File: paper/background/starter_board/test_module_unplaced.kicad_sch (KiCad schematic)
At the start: 15 parts, among them J1 Barrel_Jack_12V, M1 ERM_Motor, M2 Stepper_4wire, M3 Servo_3pin, U1 D24V22F5_Buck, U2 Pi_Pico_W, U3 DRV2605L_Breakout, U4 DRV8871_Breakout, U5 Tic_T500, U6 Waveshare_2CH_RS232

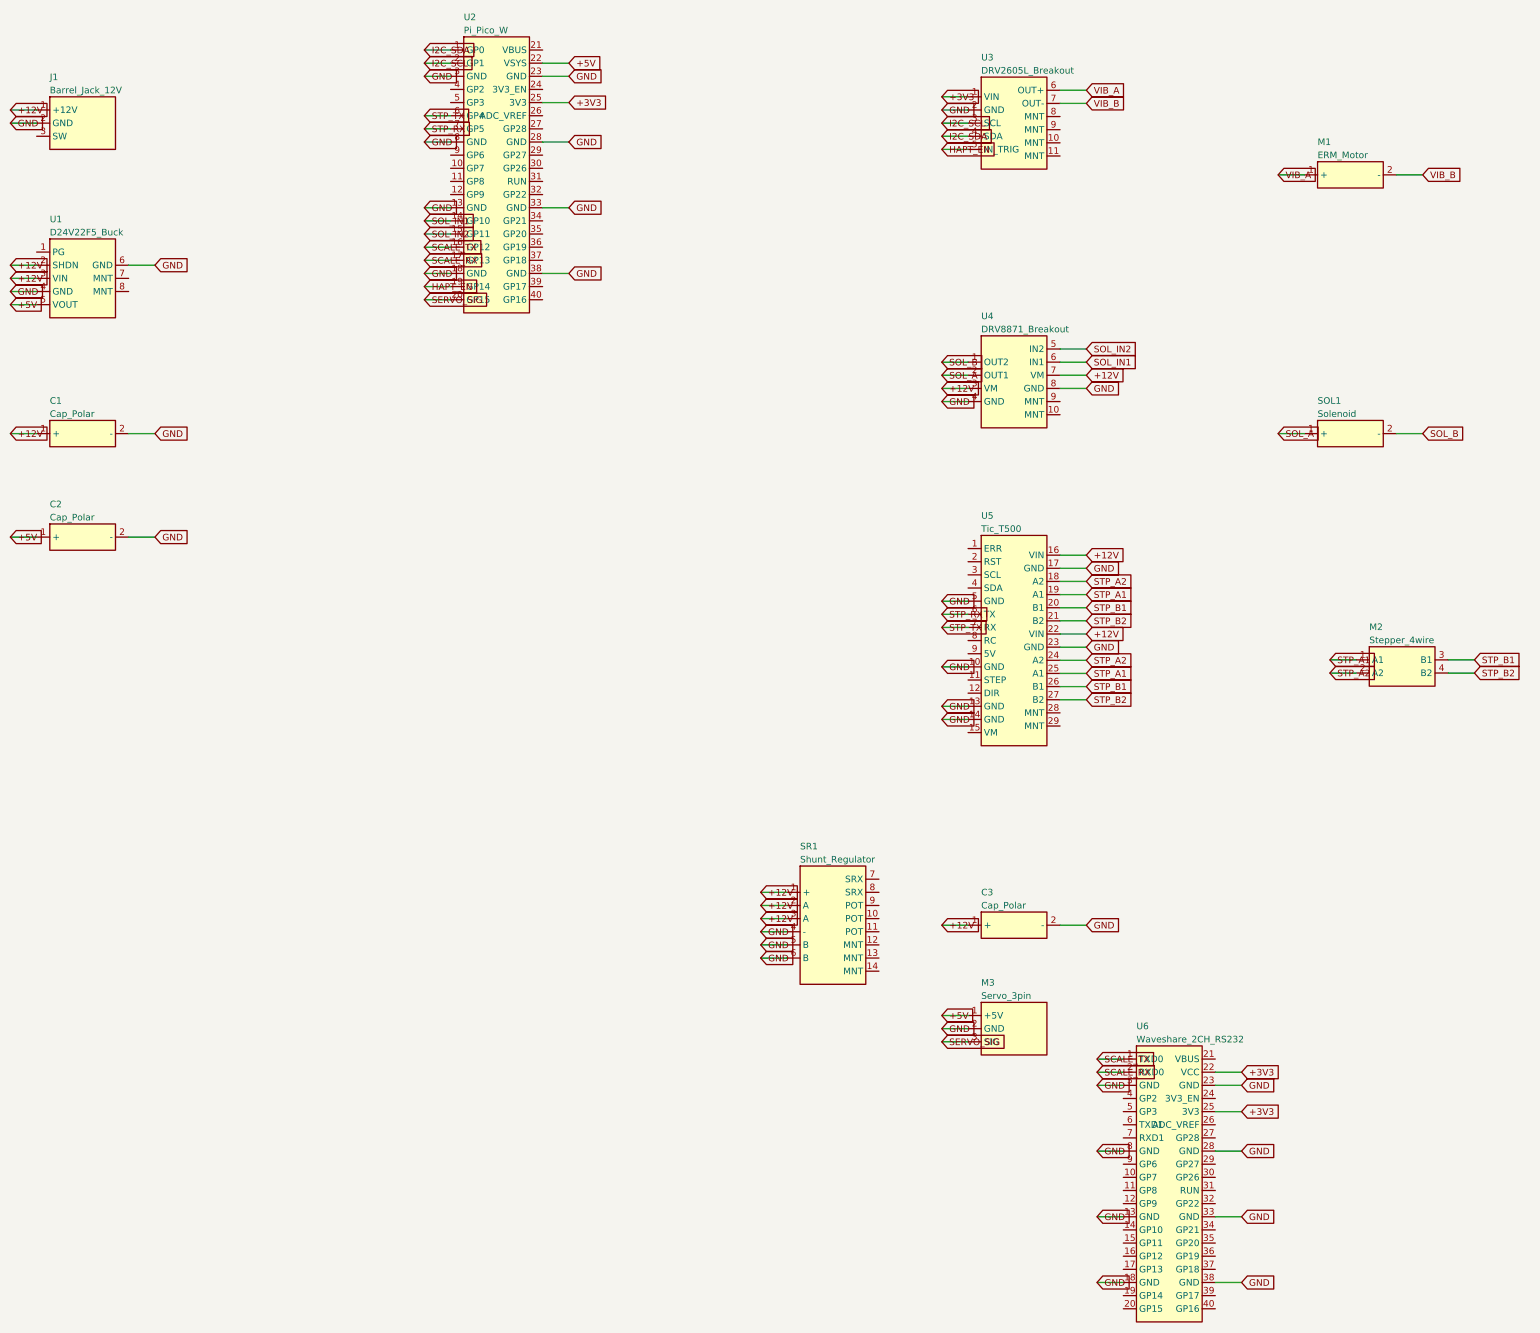
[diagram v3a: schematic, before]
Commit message: Add second dispensing-angle servo M4 (SERVO_SIG2 on GP2) — 2-servo design alignment
williamulbz's PR #76 review flagged that the board predates the move to
the 2-servo design (PR #66 dual-servo hinge; PR #100 generate.py rev C).
build_starter_board.py now emits a second 3-pin servo header M4 wired
exactly as rev C: SIG -> SERVO_SIG2 on Pico GP2 (mirrored in firmware via
config.SERVO2_INVERT), +5V/GND shared. M4 joins the logic/mcu placement
cluster beside M3, edge-biased for cable exit.

Counts: 16 footprints / 175 pads / 99 net-assigned / 23 nets (placed
outline ~162x85 mm; unplaced stays 110x110 mm at ~51% courtyard).
Verified: kicad-cli netlist 99 pins / 23 nets / zero unconnected on both
trios (SERVO_SIG2 = M4.3 <-> U2.4/GP2), pcbnew DRC clean (no courtyard/
clearance/short errors), 16<->16 footprint<->symbol UUID bijection,
byte-for-byte reproducible, KiCad 7 20221018 format kept. Both trios +
previews + summary regenerated; note 21 update block, note 24 superseded
caveat (run-2 candidates lack M4; +5V now wants 2000 mA in Quilter), and
background README updated.

Co-authored-by: Sterling G. Baird <45469701+sgbaird@users.noreply.github.com>
Co-Authored-By: Claude Fable 5 <noreply@anthropic.com>
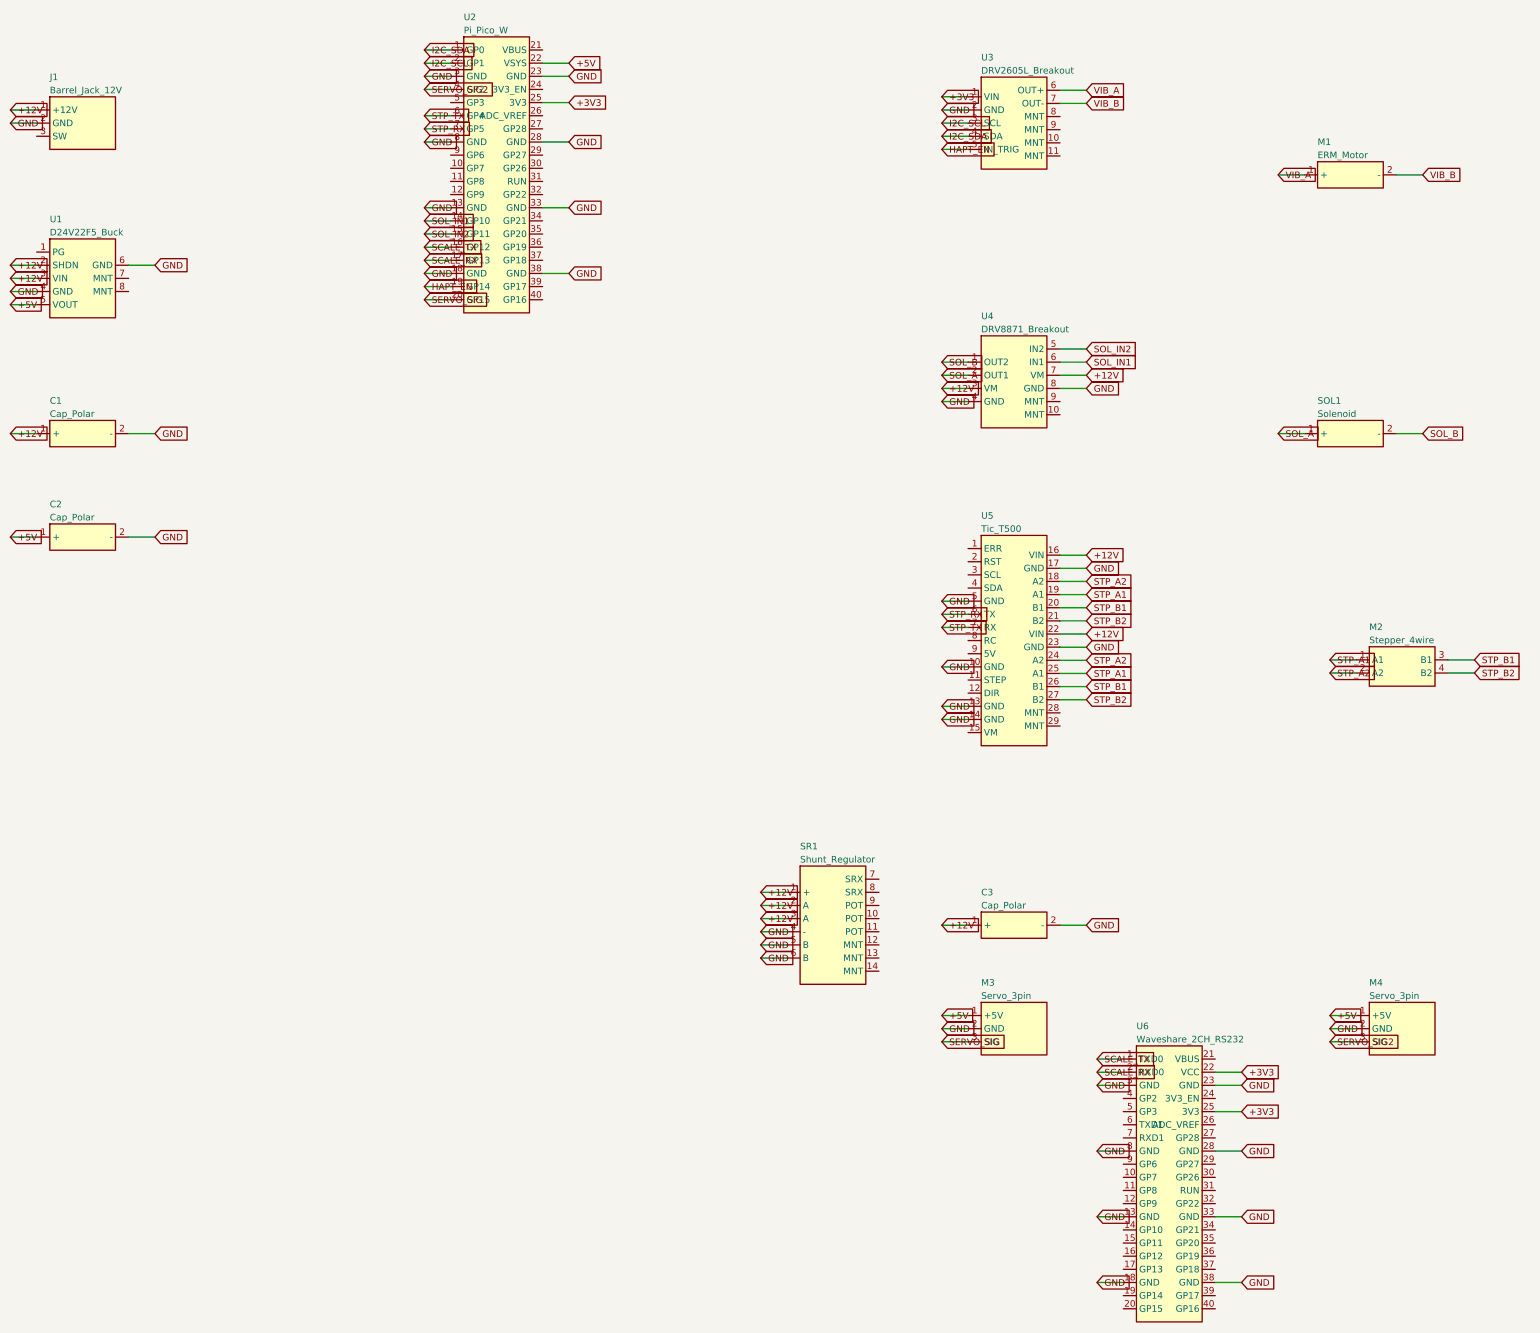
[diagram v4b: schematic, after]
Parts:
- added M4: Servo_3pin, Connector_PinHeader_2.54mm:PinHeader_1x03_P2.54mm_Vertical, symbol powder_doser_parts:Servo_3pin
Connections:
- net +5V: now also M4.1 (+5V)
- net GND: now also M4.2 (GND)
- net SERVO_SIG2: now reaches U2.4 (GP2)
- net SERVO_SIG2: now also M4.3 (SIG)
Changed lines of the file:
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@@
+    (effects (font (size 1.27 1.27)) (justify left))
+  )
+  (wire (pts (xy 101.11 33.49) (xy 96.03 33.49))
+    (stroke (width 0) (type default))
+  )
+  (global_label "SERVO_SIG2" (shape input) (at 96.03 33.49 180) (fields_autoplaced)
     (effects (font (size 1.27 1.27)) (justify left))
   )
@@
     (effects (font (size 1.27 1.27)) (justify left))
   )
+  (symbol (lib_id "powder_doser_parts:Servo_3pin") (at 285 215 0) (unit 1)
+    (in_bom yes) (on_board yes) (dnp no)
+    (property "Reference" "M4" (id 0) (at 278.65 206.11 0)
+      (effects (font (size 1.27 1.27)) (justify left)))
+    (property "Value" "Servo_3pin" (id 1) (at 278.65 208.65 0)
+      (effects (font (size 1.27 1.27)) (justify left)))
+    (property "Footprint" "Connector_PinHeader_2.54mm:PinHeader_1x03_P2.54mm_Vertical" (id 2) (at 285 215 0)
+      (effects (font (size 1.27 1.27)) hide))
+    (property "Datasheet" "" (id 3) (at 285 215 0)
+      (effects (font (size 1.27 1.27)) hide))
+    (instances
+      (project "test_module_unplaced"
+        (path "/00000000-0000-0000-0003-000000000001" (reference "M4") (unit 1))
+      )
+    )
+  )
+  (wire (pts (xy 276.11 212.46) (xy 271.03 212.46))
+    (stroke (width 0) (type default))
+  )
+  (global_label "+5V" (shape input) (at 271.03 212.46 180) (fields_autoplaced)
+    (effects (font (size 1.27 1.27)) (justify left))
+  )
+  (wire (pts (xy 276.11 215) (xy 271.03 215))
+    (stroke (width 0) (type default))
+  )
+  (global_label "GND" (shape input) (at 271.03 215 180) (fields_autoplaced)
+    (effects (font (size 1.27 1.27)) (justify left))
+  )
+  (wire (pts (xy 276.11 217.54) (xy 271.03 217.54))
+    (stroke (width 0) (type default))
+  )
+  (global_label "SERVO_SIG2" (shape input) (at 271.03 217.54 180) (fields_autoplaced)
+    (effects (font (size 1.27 1.27)) (justify left))
+  )
